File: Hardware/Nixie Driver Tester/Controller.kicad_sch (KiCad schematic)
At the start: 6 parts, among them J1 ICSP, J3 OLED

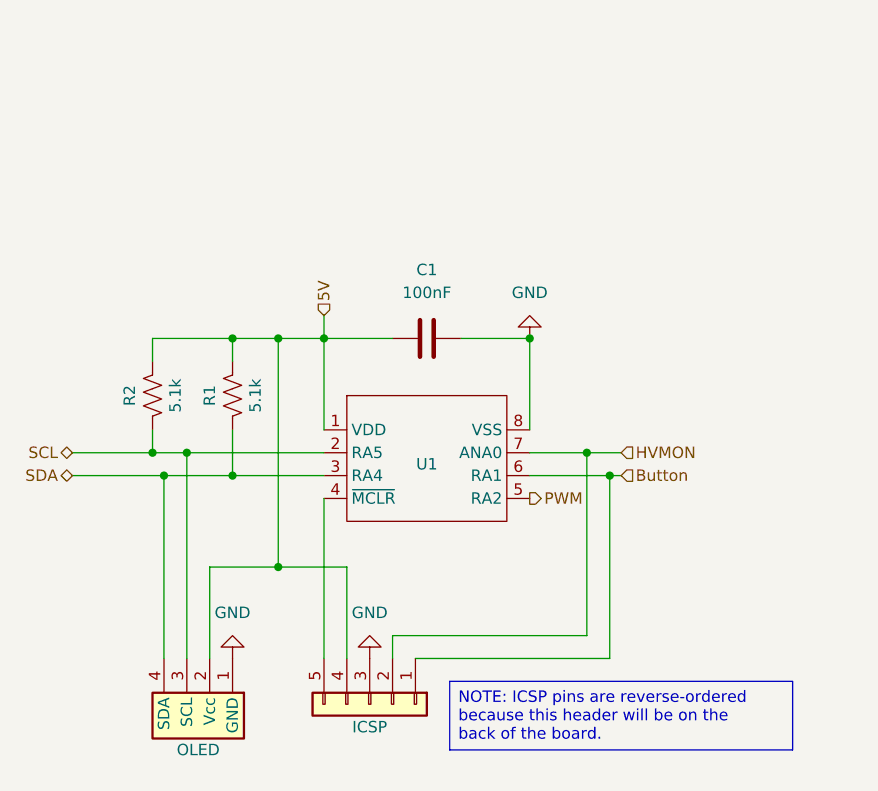
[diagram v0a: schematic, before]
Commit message: Using a STM32 instead of a PIC
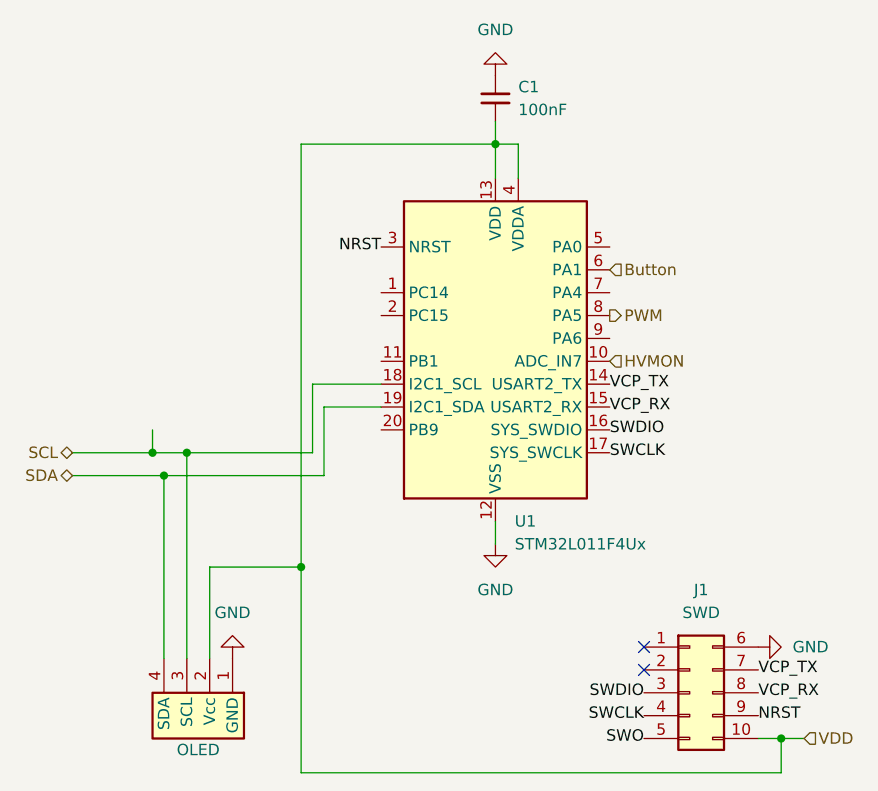
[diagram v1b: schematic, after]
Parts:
- removed C1: 100nF, Capacitor_SMD:C_0603_1608Metric, symbol Device:C
- removed J1: ICSP, Connector_PinSocket_2.54mm:PinSocket_1x05_P2.54mm_Horizontal, symbol Connector_Generic:Conn_01x05
- removed R1, R2: 5.1k, Resistor_SMD:R_0603_1608Metric, symbol Device:R_US
- removed U1: ~, Package_SO:SOIC-8_3.9x4.9mm_P1.27mm, symbol MCU_Microchip_PIC16_:PIC16F15214-I/SN
- added C1: 100nF, Capacitor_SMD:C_0603_1608Metric, symbol Device:C_Small
- added J1: SWD, Connectory_PCB_Edge_:AVX-009159010061911, symbol Connector_Generic:Conn_02x05_Top_Bottom
- added U1: STM32L011F4Ux, Package_DFN_QFN:ST_UFQFPN-20_3x3mm_P0.5mm, symbol MCU_ST_STM32L0:STM32L011F4Ux
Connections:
- net Button: now also U1.6 (PA1)
- net GND: now also C1.1, J1.6 (Pin_6), U1.12 (VSS)
- net HVMON: now also U1.10 (PA7)
- net PWM: now also U1.8 (PA5)
- net SCL: now also U1.18 (PB6)
- net SDA: now also U1.19 (PB7)
- net 5V renamed VDD
- net VDD: now also C1.2, J1.10 (Pin_10), U1.13 (VDD), U1.4 (VDDA)
- new net NRST: J1.9 (Pin_9), U1.3 (NRST)
- new net SWCLK: J1.4 (Pin_4), U1.17 (PA14)
- new net SWDIO: J1.3 (Pin_3), U1.16 (PA13)
- new net SWO: J1.5 (Pin_5)
- new net VCP_RX: J1.8 (Pin_8), U1.15 (PA10)
- new net VCP_TX: J1.7 (Pin_7), U1.14 (PA9)
- no-connect marks 0 -> 2

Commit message: Switch mode 3.3V and SMD inductor
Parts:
- renumbered J3 to J1, J1 to J2
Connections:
- net SWO: now also U1.9 (PA6)
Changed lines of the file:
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@@
+		)
+	)
+	(label "SWO"
+		(at 161.29 81.28 0)
+		(effects
+			(font
+				(size 1.27 1.27)
+			)
+			(justify left)
 		)
 	)
@@
 		(in_pos_files yes)
 		(dnp no)
-		(property "Reference" "J3"
+		(property "Reference" "J1"
 			(at 114.3 124.46 90)
 			(hide yes)
@@
 			(project "Nixie Driver Tester"
 				(path "/c2082ee6-4c2e-4b3c-b2d7-410eae192cfe/9f01134a-2f79-4022-9c4f-b5d1e4c08c6e"
-					(reference "J3")
+					(reference "J1")
 					(unit 1)
 				)
@@
 		(dnp no)
 		(fields_autoplaced yes)
-		(property "Reference" "#PWR012"
+		(property "Reference" "#PWR05"
 			(at 184.15 115.57 0)
 			(hide yes)
@@
 			(project "Nixie Driver Tester"
 				(path "/c2082ee6-4c2e-4b3c-b2d7-410eae192cfe/9f01134a-2f79-4022-9c4f-b5d1e4c08c6e"
-					(reference "#PWR012")
+					(reference "#PWR05")
 					(unit 1)
 				)
@@
 		(dnp no)
 		(fields_autoplaced yes)
-		(property "Reference" "#PWR025"
+		(property "Reference" "#PWR03"
 			(at 148.59 45.72 0)
 			(hide yes)
@@
 			(project "Nixie Driver Tester"
 				(path "/c2082ee6-4c2e-4b3c-b2d7-410eae192cfe/9f01134a-2f79-4022-9c4f-b5d1e4c08c6e"
-					(reference "#PWR025")
+					(reference "#PWR03")
 					(unit 1)
 				)
@@
 		)
 		(pin "7"
+			(alternate "LPUART1_TX")
 		)
 		(pin "9"
@@
 		(dnp no)
 		(fields_autoplaced yes)
-		(property "Reference" "#PWR010"
+		(property "Reference" "#PWR02"
 			(at 119.38 110.49 0)
 			(hide yes)
@@
 			(project "Nixie Driver Tester"
 				(path "/c2082ee6-4c2e-4b3c-b2d7-410eae192cfe/9f01134a-2f79-4022-9c4f-b5d1e4c08c6e"
-					(reference "#PWR010")
+					(reference "#PWR02")
 					(unit 1)
 				)
@@
 		(dnp no)
 		(fields_autoplaced yes)
-		(property "Reference" "J1"
+		(property "Reference" "J2"
 			(at 171.45 109.22 0)
 			(show_name no)
@@
 			(project "Nixie Driver Tester"
 				(path "/c2082ee6-4c2e-4b3c-b2d7-410eae192cfe/9f01134a-2f79-4022-9c4f-b5d1e4c08c6e"
-					(reference "J1")
+					(reference "J2")
 					(unit 1)
 				)
@@
 		(dnp no)
 		(fields_autoplaced yes)
-		(property "Reference" "#PWR018"
+		(property "Reference" "#PWR04"
 			(at 148.59 110.49 0)
 			(hide yes)
@@
 			(project "Nixie Driver Tester"
 				(path "/c2082ee6-4c2e-4b3c-b2d7-410eae192cfe/9f01134a-2f79-4022-9c4f-b5d1e4c08c6e"
-					(reference "#PWR018")
+					(reference "#PWR04")
 					(unit 1)
 				)

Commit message: Added test points
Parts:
- added TP1: SCL, TestPoint:TestPoint_Keystone_5015_Micro_Mini, symbol Connector:TestPoint
- added TP2: SDA, TestPoint:TestPoint_Keystone_5015_Micro_Mini, symbol Connector:TestPoint
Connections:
- net SCL: now also TP1.1
- net SDA: now also TP2.1
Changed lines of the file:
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@@
 	(paper "A4")
+	(junction
+		(at 105.41 96.52)
+		(diameter 0)
+		(color 0 0 0 0)
+	)
+	(junction
+		(at 105.41 93.98)
+		(diameter 0)
+		(color 0 0 0 0)
+	)
 	(junction
 		(at 127 106.68)
@@
 	)
 	(junction
-		(at 110.49 93.98)
-		(diameter 0)
-		(color 0 0 0 0)
-	)
-	(junction
 		(at 180.34 125.73)
 		(diameter 0)
@@
 	(wire
 		(pts
-			(xy 111.76 96.52) (xy 101.6 96.52)
+			(xy 111.76 96.52) (xy 105.41 96.52)
 		)
 		(stroke
@@
 	(wire
 		(pts
-			(xy 110.49 91.44) (xy 110.49 93.98)
-		)
-		(stroke
-			(width 0)
-			(type default)
-		)
-	)
-	(wire
-		(pts
 			(xy 148.59 59.69) (xy 151.13 59.69)
 		)
@@
 	(wire
 		(pts
-			(xy 101.6 93.98) (xy 110.49 93.98)
-		)
-		(stroke
-			(width 0)
-			(type default)
-		)
-	)
-	(wire
-		(pts
-			(xy 114.3 93.98) (xy 110.49 93.98)
+			(xy 105.41 93.98) (xy 114.3 93.98)
+		)
+		(stroke
+			(width 0)
+			(type default)
+		)
+	)
+	(wire
+		(pts
+			(xy 101.6 93.98) (xy 105.41 93.98)
 		)
 		(stroke
@@
 		(pts
 			(xy 127 129.54) (xy 127 106.68)
+		)
+		(stroke
+			(width 0)
+			(type default)
+		)
+	)
+	(wire
+		(pts
+			(xy 105.41 96.52) (xy 101.6 96.52)
 		)
 		(stroke
@@
 	)
 	(symbol
+		(lib_id "Connector:TestPoint")
+		(at 105.41 93.98 0)
+		(unit 1)
+		(body_style 1)
+		(exclude_from_sim no)
+		(in_bom yes)
+		(on_board yes)
+		(in_pos_files yes)
+		(dnp no)
+		(property "Reference" "TP1"
+			(at 105.41 88.9 0)
+			(show_name no)
+			(do_not_autoplace no)
+			(effects
+				(font
+					(size 1.27 1.27)
+				)
+				(justify bottom)
+			)
+		)
+		(property "Value" "SCL"
+			(at 107.95 91.9479 0)
+			(hide yes)
+			(show_name no)
+			(do_not_autoplace no)
+			(effects
+				(font
+					(size 1.27 1.27)
+				)
+				(justify left)
+			)
+		)
+		(property "Footprint" "TestPoint:TestPoint_Keystone_5015_Micro_Mini"
+			(at 110.49 93.98 0)
+			(hide yes)
+			(show_name no)
+			(do_not_autoplace no)
+			(effects
+				(font
+					(size 1.27 1.27)
+				)
+			)
+		)
+		(property "Datasheet" ""
+			(at 110.49 93.98 0)
+			(hide yes)
+			(show_name no)
+			(do_not_autoplace no)
+			(effects
+				(font
+					(size 1.27 1.27)
+				)
+			)
+		)
+		(property "Description" "test point"
+			(at 105.41 93.98 0)
+			(hide yes)
+			(show_name no)
+			(do_not_autoplace no)
+			(effects
+				(font
+					(size 1.27 1.27)
+				)
+			)
+		)
+		(pin "1"
+		)
+		(instances
+			(project "Nixie Driver Tester"
+				(path "/c2082ee6-4c2e-4b3c-b2d7-410eae192cfe/9f01134a-2f79-4022-9c4f-b5d1e4c08c6e"
+					(reference "TP1")
+					(unit 1)
+				)
+			)
+		)
+	)
+	(symbol
 		(lib_id "power:GND")
 		(at 148.59 52.07 180)
@@
 					(unit 1)
 				)
+			)
+		)
+	)
+	(symbol
+		(lib_id "Connector:TestPoint")
+		(at 105.41 96.52 180)
+		(unit 1)
+		(body_style 1)
+		(exclude_from_sim no)
+		(in_bom yes)
+		(on_board yes)
+		(in_pos_files yes)
+		(dnp no)
+		(property "Reference" "TP2"
+			(at 105.41 101.6 0)
+			(show_name no)
+			(do_not_autoplace no)
+			(effects
+				(font
+					(size 1.27 1.27)
+				)
+				(justify bottom)
+			)
+		)
+		(property "Value" "SDA"
+			(at 102.87 98.5521 0)
+			(hide yes)
+			(show_name no)
+			(do_not_autoplace no)
+			(effects
+				(font
+					(size 1.27 1.27)
+				)
+				(justify left)
+			)
+		)
+		(property "Footprint" "TestPoint:TestPoint_Keystone_5015_Micro_Mini"
+			(at 100.33 96.52 0)
+			(hide yes)
+			(show_name no)
+			(do_not_autoplace no)
+			(effects
+				(font
+					(size 1.27 1.27)
+				)
+			)
+		)
+		(property "Datasheet" ""
+			(at 100.33 96.52 0)
+			(hide yes)
+			(show_name no)
+			(do_not_autoplace no)
+			(effects
+				(font
+					(size 1.27 1.27)
+				)
+			)
+		)
+		(property "Description" "test point"
+			(at 105.41 96.52 0)
+			(hide yes)
+			(show_name no)
+			(do_not_autoplace no)
+			(effects
+				(font
+					(size 1.27 1.27)
+				)
+			)
+		)
+		(pin "1"
+		)
+		(instances
+			(project "Nixie Driver Tester"
+				(path "/c2082ee6-4c2e-4b3c-b2d7-410eae192cfe/9f01134a-2f79-4022-9c4f-b5d1e4c08c6e"
+					(reference "TP2")
+					(unit 1)
+				)

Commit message: New driver interface
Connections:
- net HVMON: now also U1.8 (PA5); no longer U1.10 (PA7)
- net PWM: now also U1.10 (PA7); no longer U1.8 (PA5)
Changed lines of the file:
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@@
 	(hierarchical_label "PWM"
 		(shape output)
-		(at 161.29 78.74 0)
+		(at 161.29 83.82 0)
 		(effects
 			(font
@@
 	(hierarchical_label "HVMON"
 		(shape input)
-		(at 161.29 83.82 0)
+		(at 161.29 78.74 0)
 		(effects
 			(font
@@
 		)
 		(pin "8"
+			(alternate "ADC_IN5")
 		)
 		(pin "13"
@@
 		)
 		(pin "10"
-			(alternate "ADC_IN7")
 		)
 		(pin "17"

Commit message: New MOSFET and driver IC
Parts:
- added TP3: PWM, TestPoint:TestPoint_Keystone_5015_Micro_Mini, symbol Connector:TestPoint
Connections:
- net PWM: now also TP3.1
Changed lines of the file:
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@@
+	)
+	(junction
+		(at 177.8 83.82)
+		(diameter 0)
+		(color 0 0 0 0)
 	)
 	(junction
@@
 	(wire
 		(pts
+			(xy 177.8 83.82) (xy 161.29 83.82)
+		)
+		(stroke
+			(width 0)
+			(type default)
+		)
+	)
+	(wire
+		(pts
 			(xy 128.27 86.36) (xy 128.27 93.98)
 		)
@@
 		(pts
 			(xy 127 106.68) (xy 116.84 106.68)
+		)
+		(stroke
+			(width 0)
+			(type default)
+		)
+	)
+	(wire
+		(pts
+			(xy 187.96 83.82) (xy 177.8 83.82)
 		)
 		(stroke
@@
 	(hierarchical_label "PWM"
 		(shape output)
-		(at 161.29 83.82 0)
+		(at 187.96 83.82 0)
 		(effects
 			(font
@@
 					(unit 1)
 				)
+			)
+		)
+	)
+	(symbol
+		(lib_id "Connector:TestPoint")
+		(at 177.8 83.82 0)
+		(unit 1)
+		(body_style 1)
+		(exclude_from_sim no)
+		(in_bom yes)
+		(on_board yes)
+		(in_pos_files yes)
+		(dnp no)
+		(property "Reference" "TP3"
+			(at 177.8 78.74 0)
+			(show_name no)
+			(do_not_autoplace no)
+			(effects
+				(font
+					(size 1.27 1.27)
+				)
+				(justify bottom)
+			)
+		)
+		(property "Value" "PWM"
+			(at 180.34 81.7879 0)
+			(hide yes)
+			(show_name no)
+			(do_not_autoplace no)
+			(effects
+				(font
+					(size 1.27 1.27)
+				)
+				(justify left)
+			)
+		)
+		(property "Footprint" "TestPoint:TestPoint_Keystone_5015_Micro_Mini"
+			(at 182.88 83.82 0)
+			(hide yes)
+			(show_name no)
+			(do_not_autoplace no)
+			(effects
+				(font
+					(size 1.27 1.27)
+				)
+			)
+		)
+		(property "Datasheet" ""
+			(at 182.88 83.82 0)
+			(hide yes)
+			(show_name no)
+			(do_not_autoplace no)
+			(effects
+				(font
+					(size 1.27 1.27)
+				)
+			)
+		)
+		(property "Description" "test point"
+			(at 177.8 83.82 0)
+			(hide yes)
+			(show_name no)
+			(do_not_autoplace no)
+			(effects
+				(font
+					(size 1.27 1.27)
+				)
+			)
+		)
+		(pin "1"
+		)
+		(instances
+			(project "Nixie Driver Tester"
+				(path "/c2082ee6-4c2e-4b3c-b2d7-410eae192cfe/9f01134a-2f79-4022-9c4f-b5d1e4c08c6e"
+					(reference "TP3")
+					(unit 1)
+				)

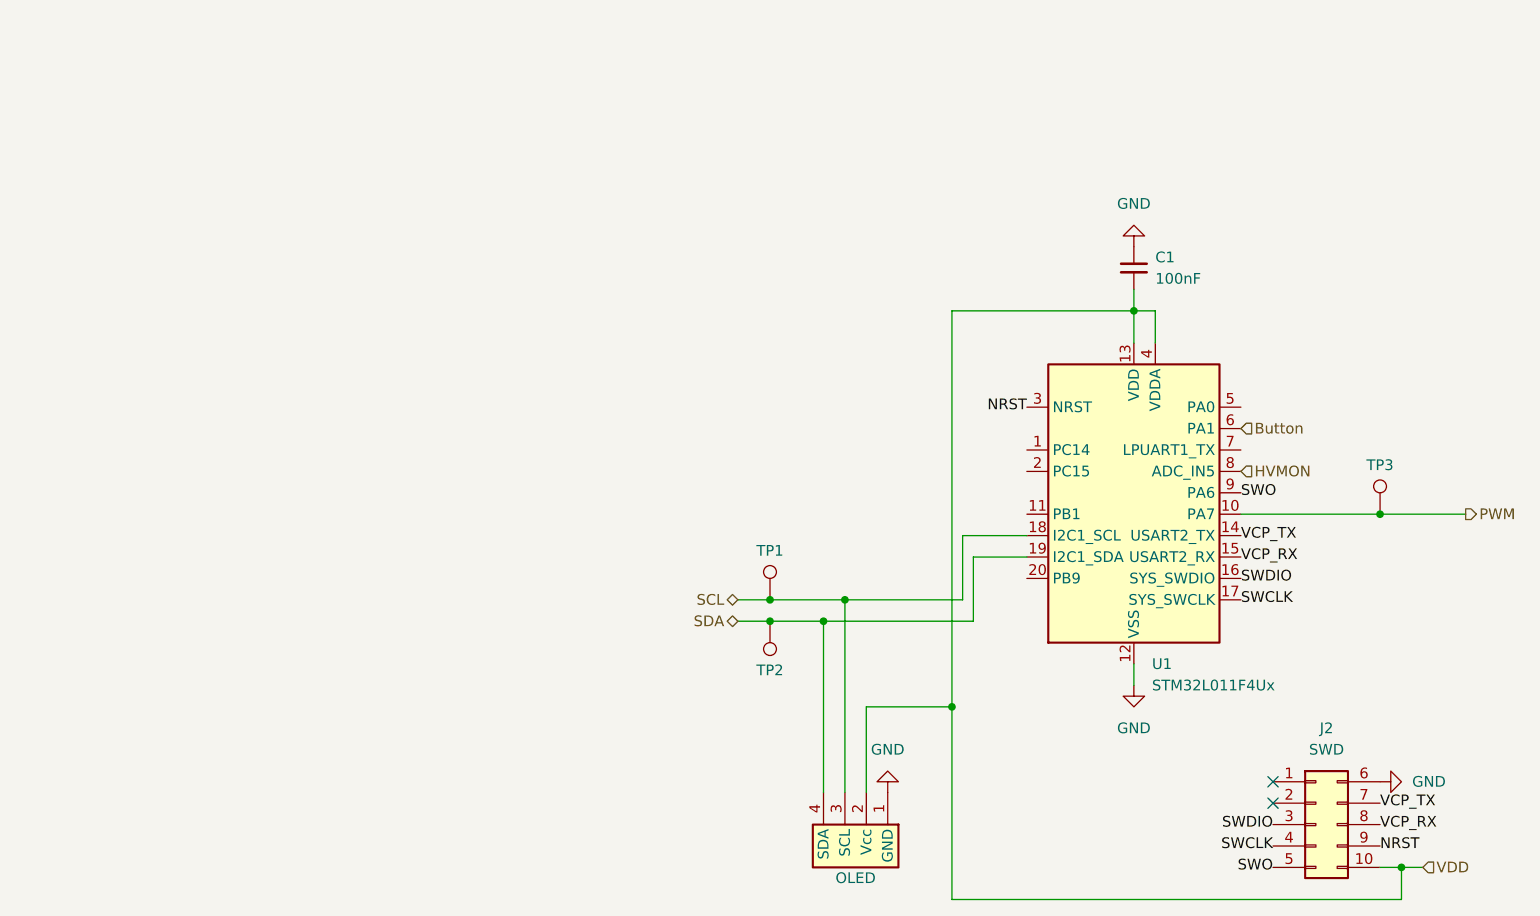
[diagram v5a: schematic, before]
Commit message: switch MCU to SMT32C5
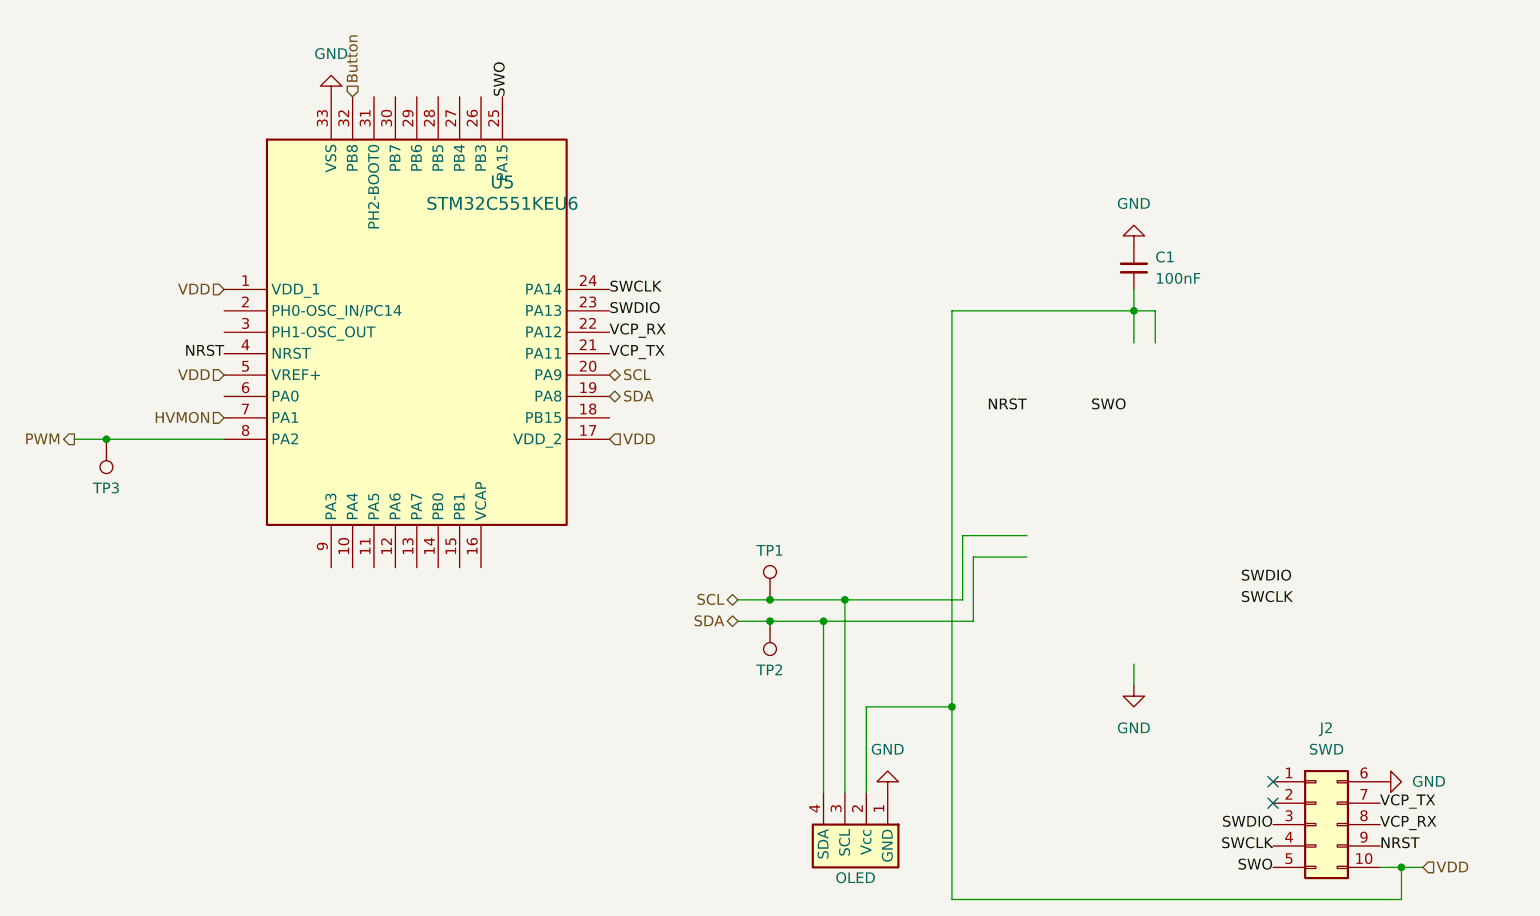
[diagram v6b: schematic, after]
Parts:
- removed U1: STM32L011F4Ux, Package_DFN_QFN:ST_UFQFPN-20_3x3mm_P0.5mm, symbol MCU_ST_STM32L0:STM32L011F4Ux
- added U5: STM32C551KEU6, Package_DFN_QFN:UFQFPN-32-1EP_5x5mm_P0.5mm_EP3.5x3.5mm, symbol MCU_ST_STM32C5_:STM32C551KEU6
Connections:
- net Button: now also U5.32 (PB8)
- net GND: now also U5.33 (VSS)
- net HVMON: now also U5.7 (PA1)
- net NRST: now also U5.4 (NRST)
- net PWM: now also U5.8 (PA2)
- net SCL: now also U5.20 (PA9)
- net SDA: now also U5.19 (PA8)
- net SWCLK: now also U5.24 (PA14)
- net SWDIO: now also U5.23 (PA13)
- net SWO: now also U5.25 (PA15)
- net VCP_RX: now also U5.22 (PA12)
- net VCP_TX: now also U5.21 (PA11)
- net VDD: now also U5.1 (VDD_1), U5.17 (VDD_2), U5.5 (VREF+)
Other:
- moved on the sheet: TP3
